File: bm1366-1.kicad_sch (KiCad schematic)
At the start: 54 parts, among them U1 25MHz, U10 AP7331, U11 AP7331, U12 BM1368_mode1, U28 BM1368_mode1

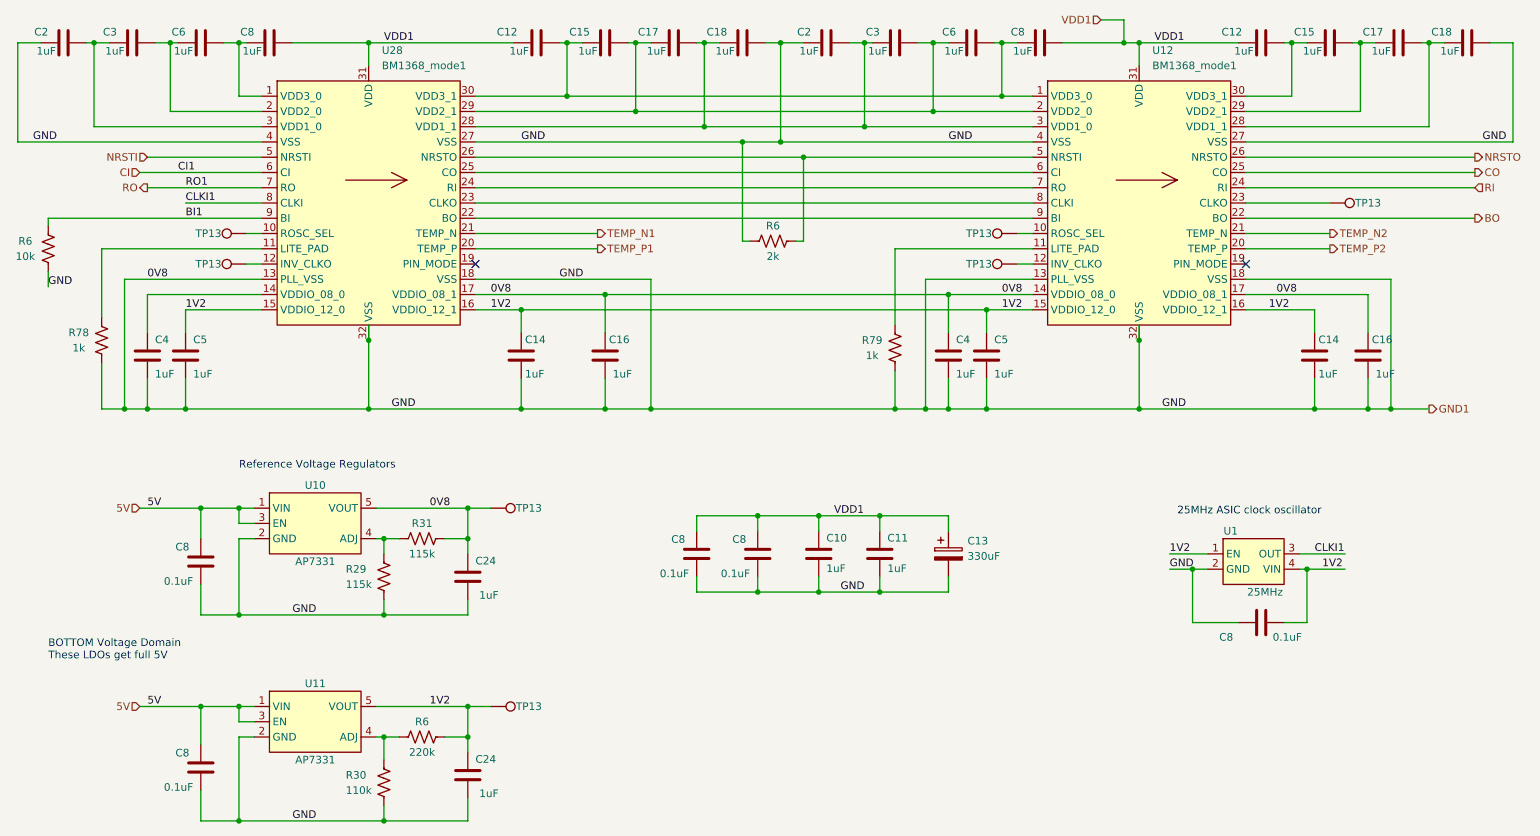
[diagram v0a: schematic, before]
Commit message: -Reset to 1V8/0V8 setup -Add TVS protection
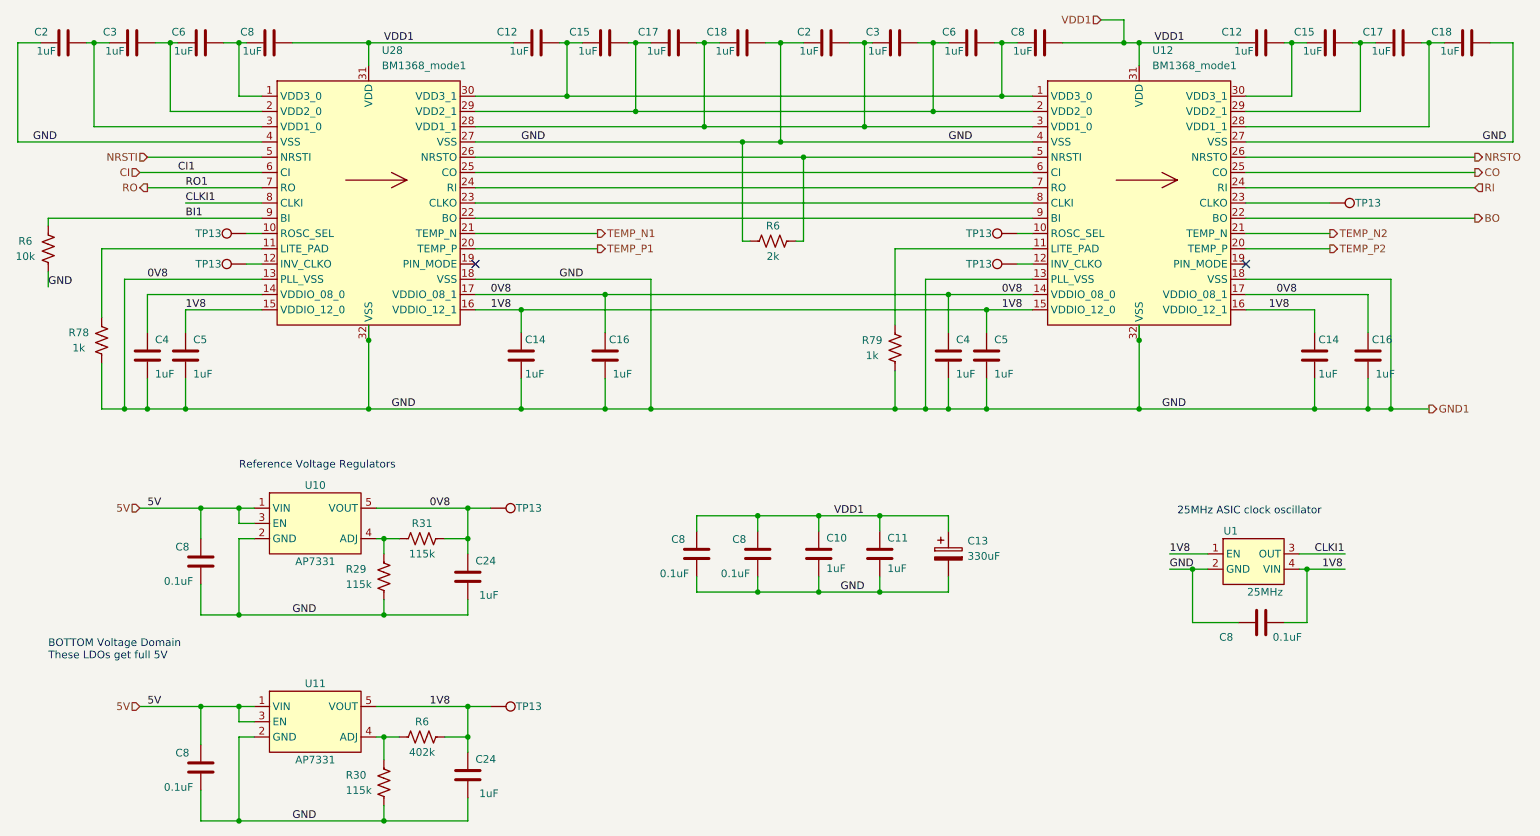
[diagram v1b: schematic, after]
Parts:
- R30: value 110k -> 115k; DK 311-110KLRTR-ND -> YAG2956CT-ND; PARTNO RC0402FR-07110KL -> RC0402FR-07115KL
- R6: value 220k -> 402k; DK 311-220KLRTR-ND -> YAG3151CT-ND; PARTNO RC0402FR-07220KL -> RC0402FR-07402KL
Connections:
- net 1V2 renamed 1V8
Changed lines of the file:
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@@
 		)
 	)
-	(label "1V2"
+	(label "1V8"
 		(at 205.74 151.13 0)
 		(fields_autoplaced yes)
@@
 		)
 	)
-	(label "1V2"
+	(label "1V8"
 		(at 92.71 110.49 0)
 		(fields_autoplaced yes)
@@
 		)
 	)
-	(label "1V2"
+	(label "1V8"
 		(at 231.14 153.67 0)
 		(fields_autoplaced yes)
@@
 		)
 	)
-	(label "1V2"
+	(label "1V8"
 		(at 82.55 176.53 0)
 		(fields_autoplaced yes)
@@
 		)
 	)
-	(label "1V2"
+	(label "1V8"
 		(at 41.91 110.49 0)
 		(fields_autoplaced yes)
@@
 		)
 	)
-	(label "1V2"
+	(label "1V8"
 		(at 177.8 110.49 0)
 		(fields_autoplaced yes)
@@
 		)
 	)
-	(label "1V2"
+	(label "1V8"
 		(at 222.25 110.49 0)
 		(fields_autoplaced yes)
@@
 			)
 		)
-		(property "Value" "220k"
+		(property "Value" "402k"
 			(at 81.28 184.15 90)
 			(effects
@@
 			)
 		)
-		(property "DK" "311-220KLRTR-ND"
+		(property "DK" "YAG3151CT-ND"
 			(at 81.28 181.61 0)
 			(effects
@@
 			)
 		)
-		(property "PARTNO" "RC0402FR-07220KL"
+		(property "PARTNO" "RC0402FR-07402KL"
 			(at 81.28 181.61 0)
 			(effects
@@
 			)
 		)
-		(property "Value" "110k"
+		(property "Value" "115k"
 			(at 68.58 190.5 0)
 			(effects
@@
 			)
 		)
-		(property "DK" "311-110KLRTR-ND"
+		(property "DK" "YAG2956CT-ND"
 			(at 74.93 189.23 0)
 			(effects
@@
 			)
 		)
-		(property "PARTNO" "RC0402FR-07110KL"
+		(property "PARTNO" "RC0402FR-07115KL"
 			(at 74.93 189.23 0)
 			(effects

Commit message: updated to KiCad v9, filled in incomplete BOM and exported.
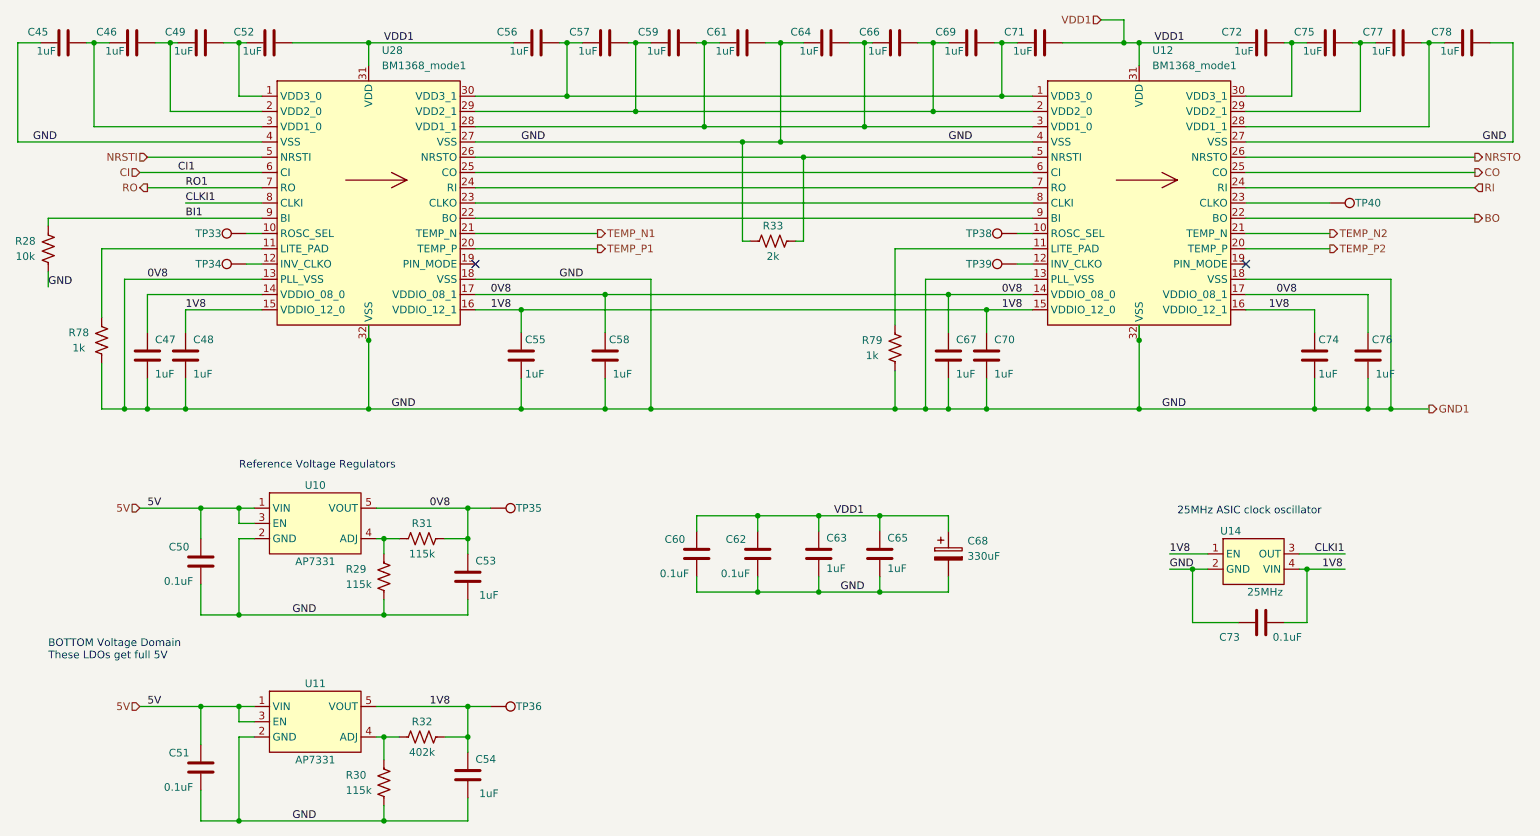
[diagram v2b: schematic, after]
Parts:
- renumbered C2 to C45, C3 to C46, C4 to C47, C5 to C48, C6 to C49, C8 to C50, C8 to C51, C8 to C52, C24 to C53, C24 to C54, C14 to C55, C12 to C56, C15 to C57, C16 to C58, C17 to C59, C8 to C60, C18 to C61, C8 to C62, C10 to C63, C2 to C64, C11 to C65, C3 to C66, C4 to C67, C13 to C68, C6 to C69, C5 to C70, C8 to C71, C12 to C72, C8 to C73, C14 to C74, C15 to C75, C16 to C76, C17 to C77, C18 to C78, R6 to R28, R6 to R32, R6 to R33, TP13 to TP33, TP13 to TP34, TP13 to TP35, TP13 to TP36, TP13 to TP38, TP13 to TP39, TP13 to TP40, U1 to U14
